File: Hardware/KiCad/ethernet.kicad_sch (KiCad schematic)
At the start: 12 parts, among them J2 RJ45_Hanrun_HR911105A_Horizon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, J3 RJ45_Hanrun_HR911105A_Horizon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, J4 RJ45_Hanrun_HR911105A_Horizon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

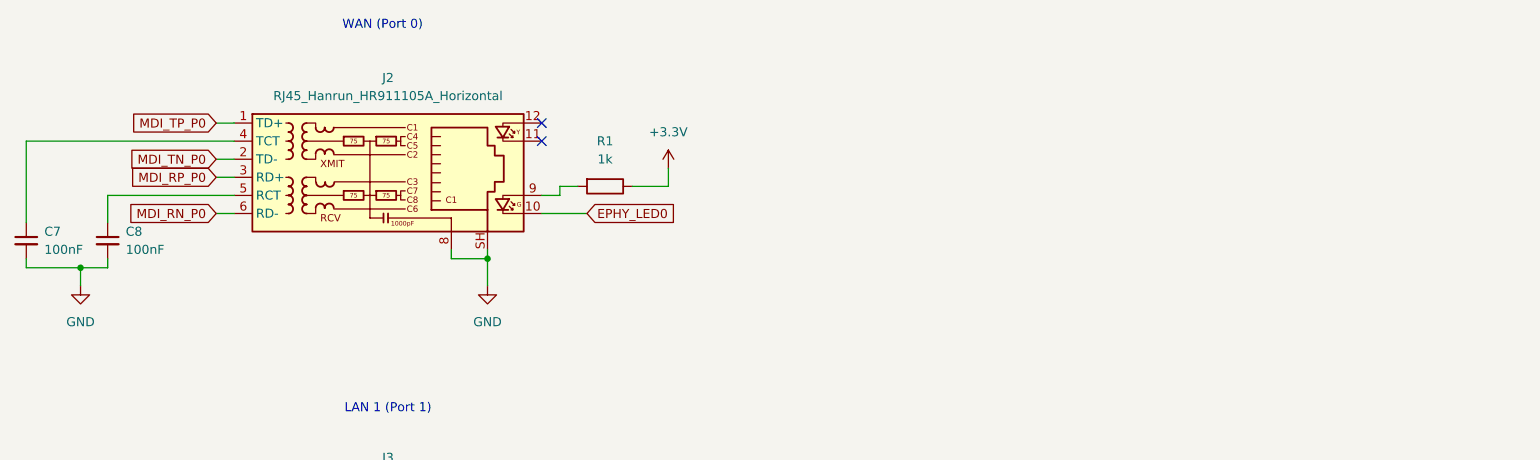
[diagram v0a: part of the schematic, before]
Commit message: USB_Bridge: add transformerless connection between usb bridge and SOM
- Ethernet: Add fourth rj45 jack
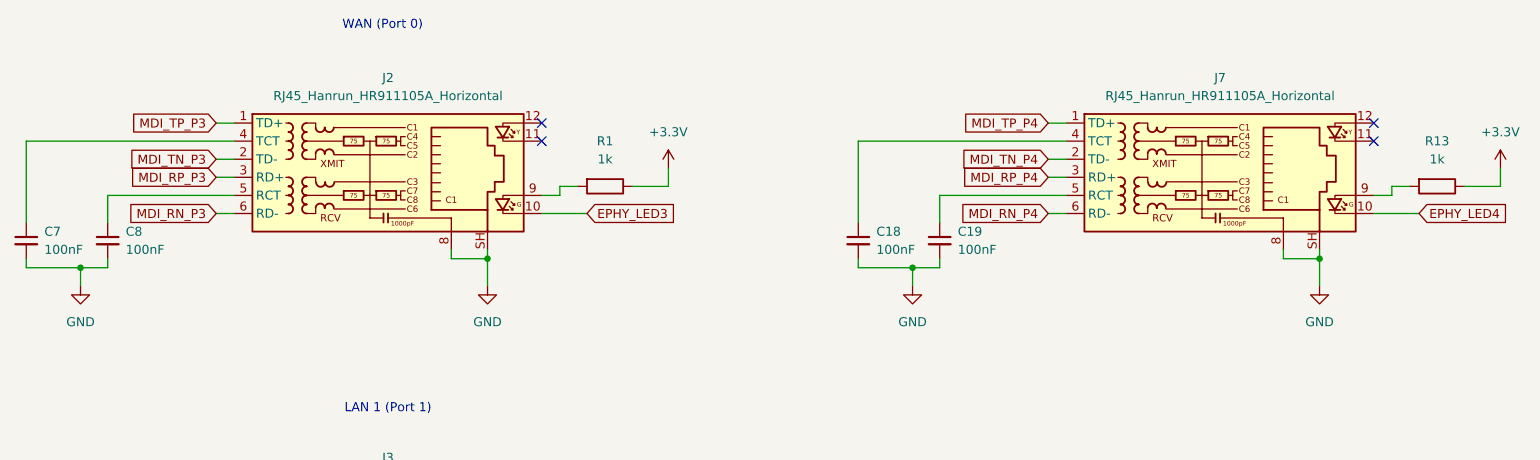
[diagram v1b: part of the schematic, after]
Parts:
- added C18, C19: 100nF, Capacitor_SMD:C_0603_1608Metric, symbol Device:C_Small
- added J7: RJ45_Hanrun_HR911105A_Horizontal, Connector_RJ:RJ45_Hanrun_HR911105A_Horizontal, symbol Connector:RJ45_Hanrun_HR911105A_Horizontal
- added R13: 1k, Resistor_SMD:R_0402_1005Metric_Pad0.72x0.64mm_HandSolder, symbol Device:R
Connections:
- net +3.3V: now also R13.1
- net GND: now also C18.2, C19.2, J7.8, J7.SH
- net EPHY_LED0 renamed EPHY_LED3
- net MDI_RN_P0 renamed MDI_RN_P3
- net MDI_RP_P0 renamed MDI_RP_P3
- net MDI_TN_P0 renamed MDI_TN_P3
- net MDI_TP_P0 renamed MDI_TP_P3
- new net: C19.1, J7.5 (RCT)
- new net: C18.1, J7.4 (TCT)
- new net: J7.9, R13.2
- new net EPHY_LED4: J7.10
- new net MDI_RN_P4: J7.6 (RD-)
- new net MDI_RP_P4: J7.3 (RD+)
- new net MDI_TN_P4: J7.2 (TD-)
- new net MDI_TP_P4: J7.1 (TD+)
- no-connect marks 6 -> 8

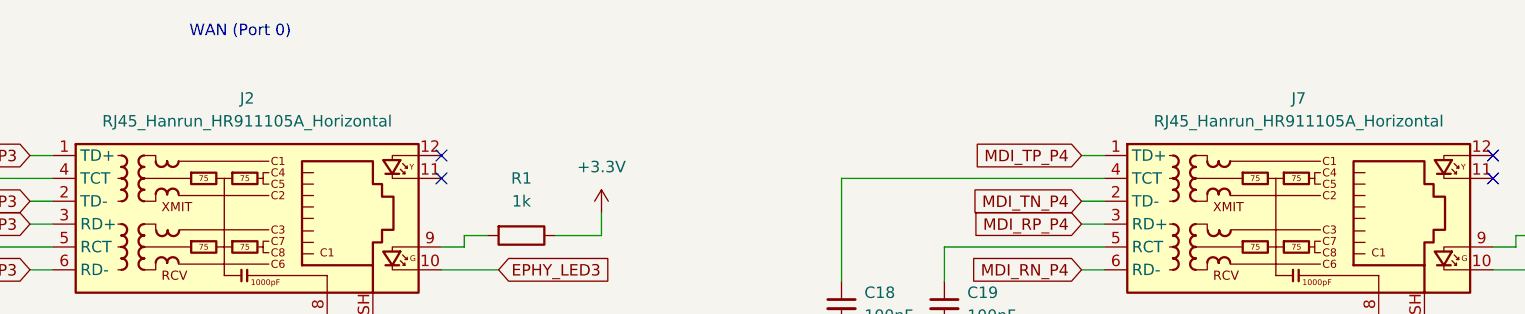
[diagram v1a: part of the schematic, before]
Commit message: Add Mini PCIe slot TE 2041626 Add Mini PCIe mounting holes and board mounting holes Add nano SIM card slot SIM8066 Add SIM ESD and EMI filter EMIF03-SIM02M8 Add USB Hub USB2422 Add USB A port with ESD chip Add README.md for details about HLK-7628N Edit text above ethernet ports
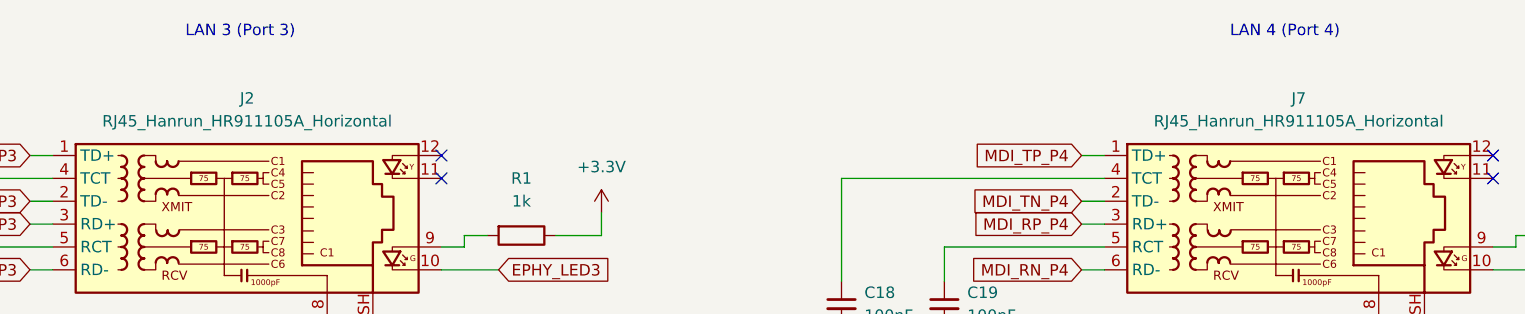
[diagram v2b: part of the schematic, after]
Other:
- note added: "LAN 3 (Port 3)"
- note added: "LAN 4 (Port 4)"
- note removed: "WAN (Port 0)"
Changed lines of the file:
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@@
 	(generator_version "10.0")
 	(paper "A4")
-	(text "WAN (Port 0)"
+	(text "LAN 3 (Port 3)"
 		(exclude_from_sim no)
 		(at 108.458 24.384 0)
@@
 		(effects
 			(font
+				(size 1.27 1.27)
+			)
+		)
+	)
+	(text "LAN 4 (Port 4)"
+		(exclude_from_sim no)
+		(at 224.536 24.384 0)
+		(effects
+			(font

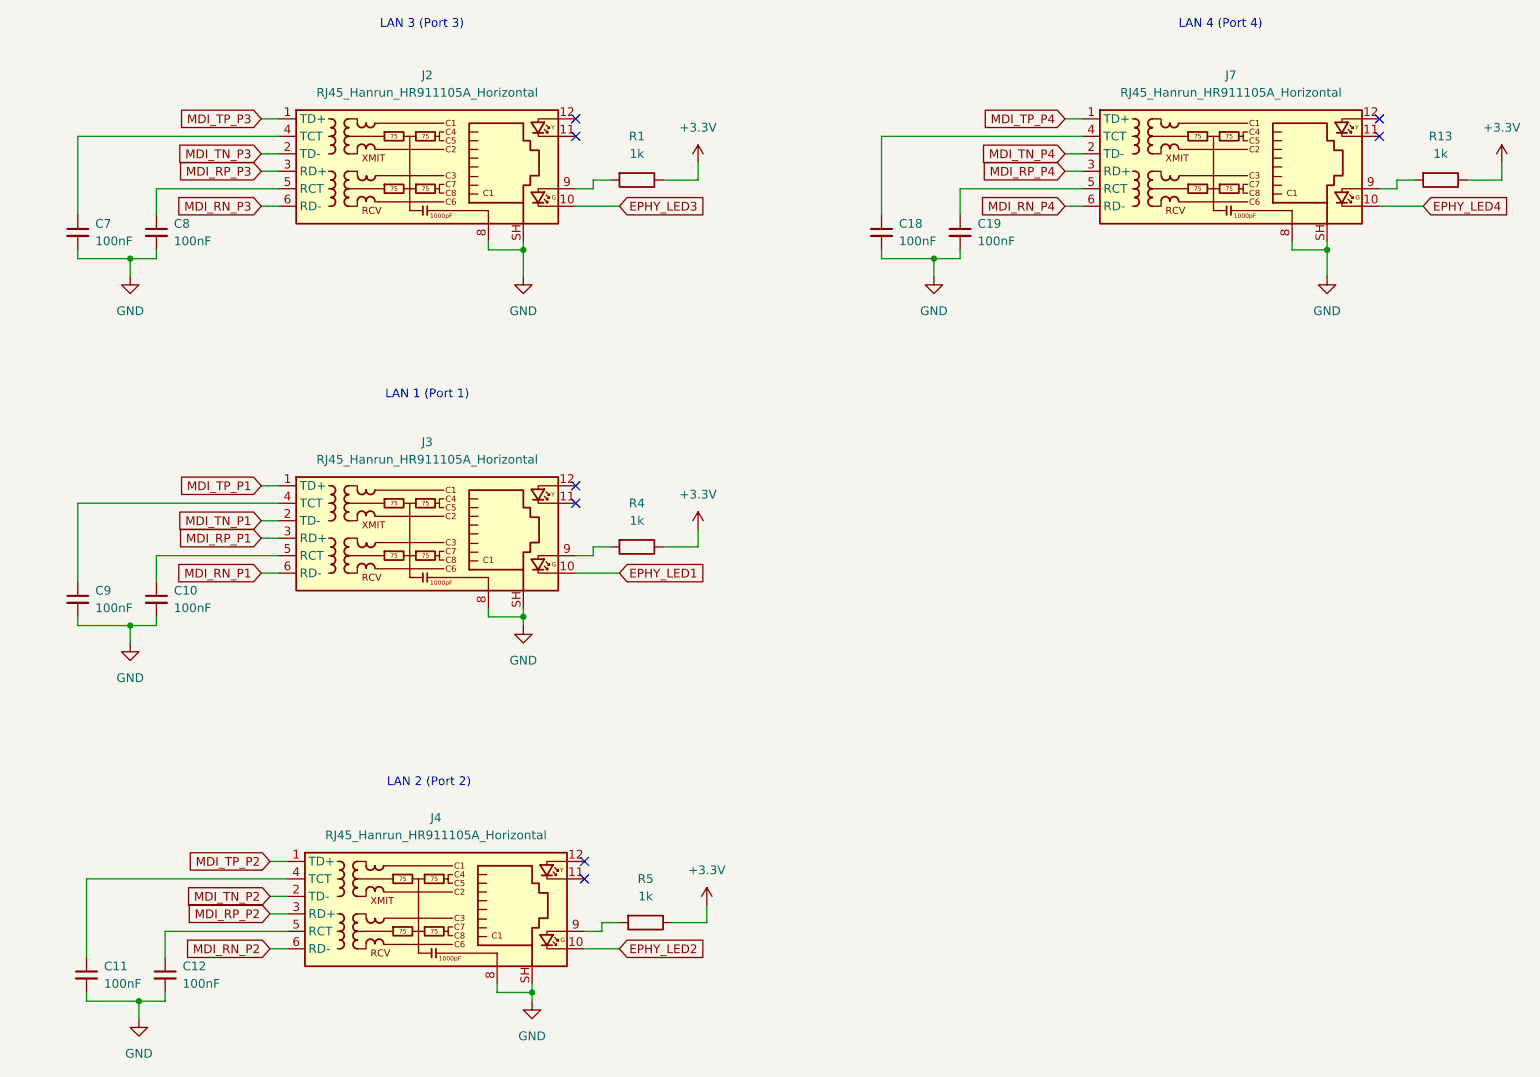
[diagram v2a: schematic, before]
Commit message: Add switches for cpu reset and watchdog reset Add swtich for WWAN wirless disable Fix USB2422 VBUS-DET and NON_REM strap pins
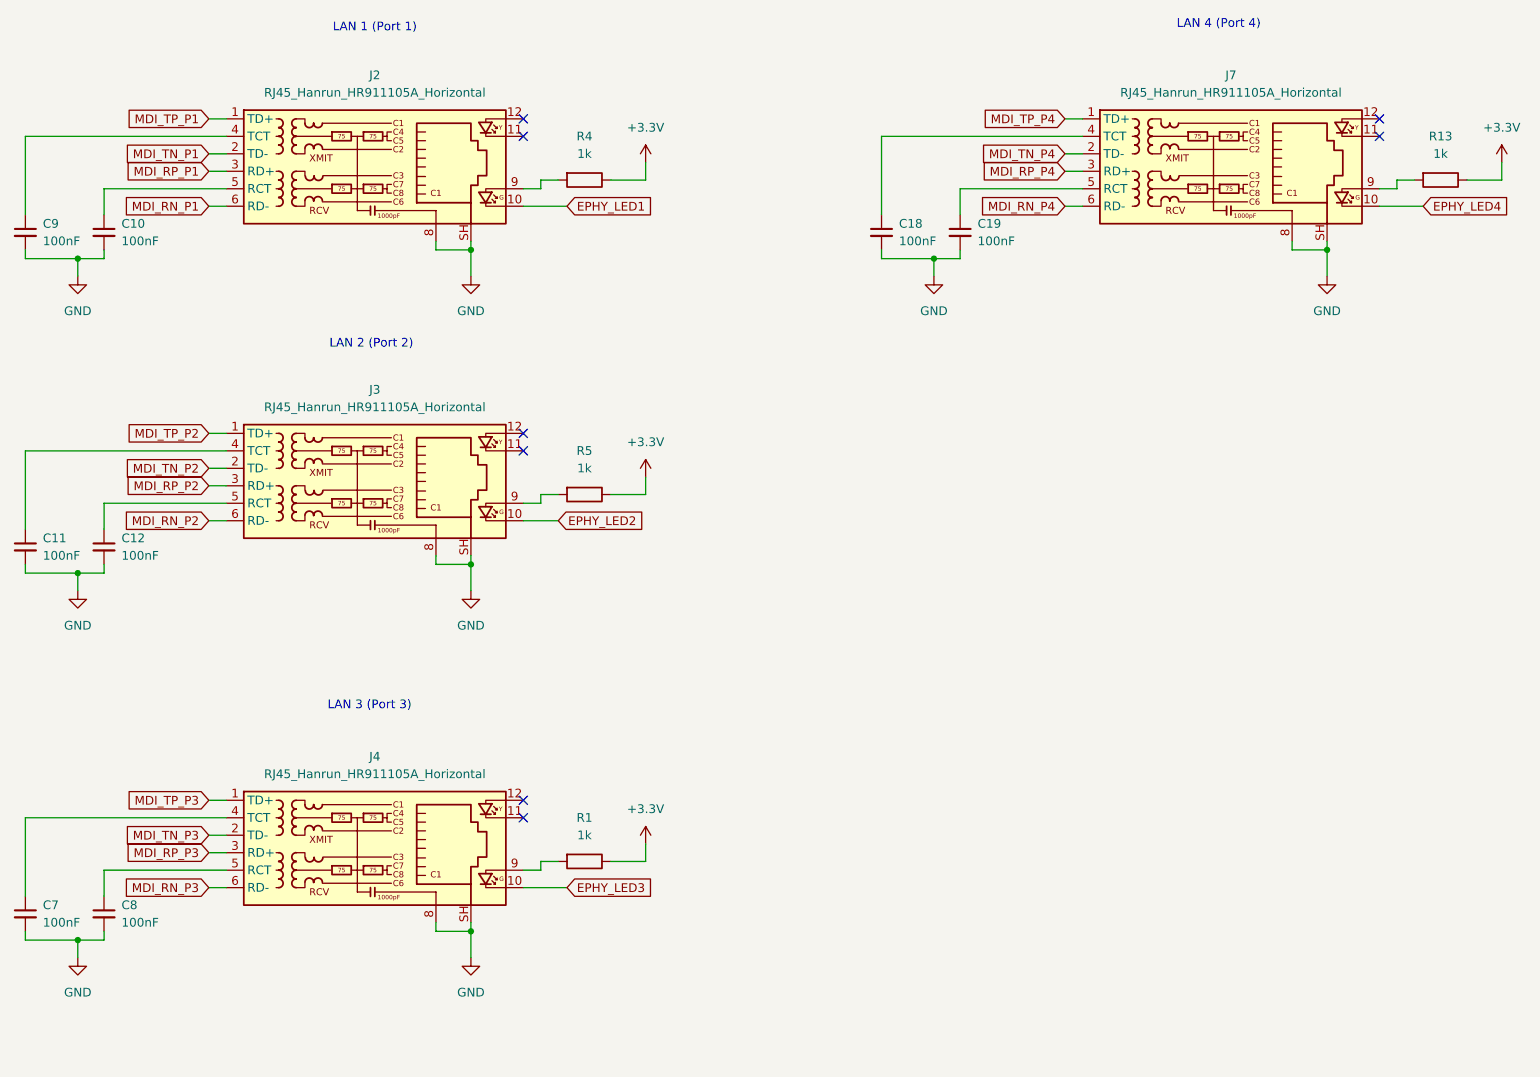
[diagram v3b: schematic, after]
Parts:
- renumbered J3 to J2, J4 to J3, J2 to J4
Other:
- moved on the sheet: C10, C11, C12, C7, C8, C9, J2, J3, J4, R1, R4, R5
